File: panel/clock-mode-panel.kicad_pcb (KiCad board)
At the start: 2 copper layers, 40.3 x 128.5 mm, 0 parts

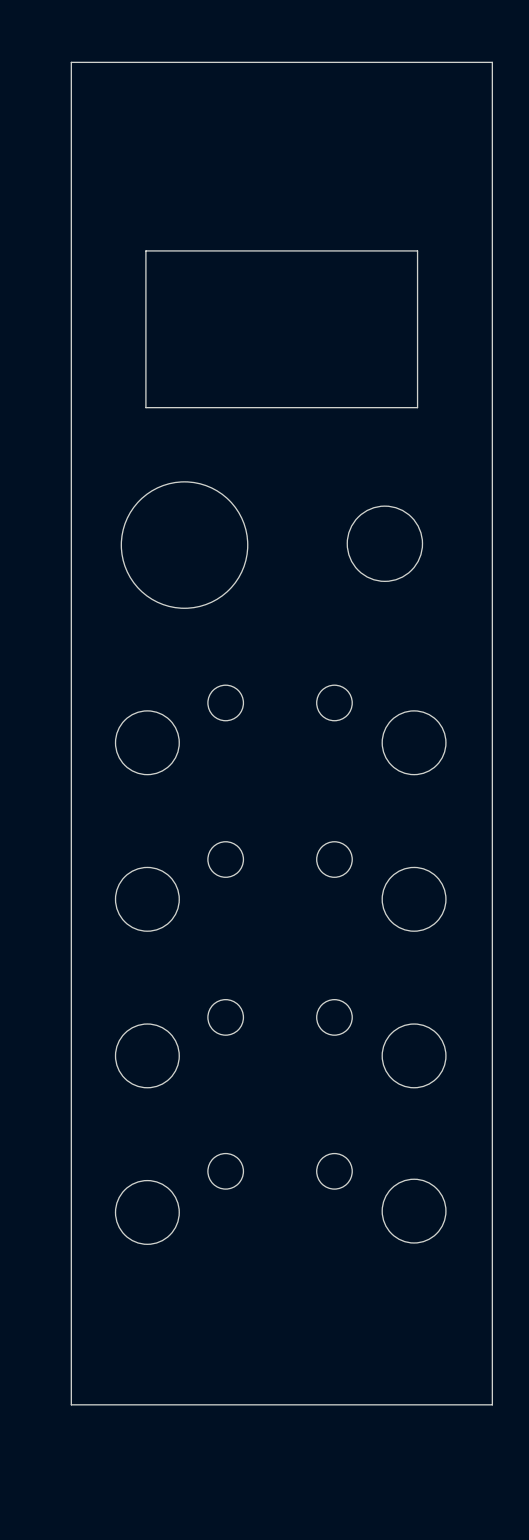
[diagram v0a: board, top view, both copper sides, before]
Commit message: feat: add artwork to panel
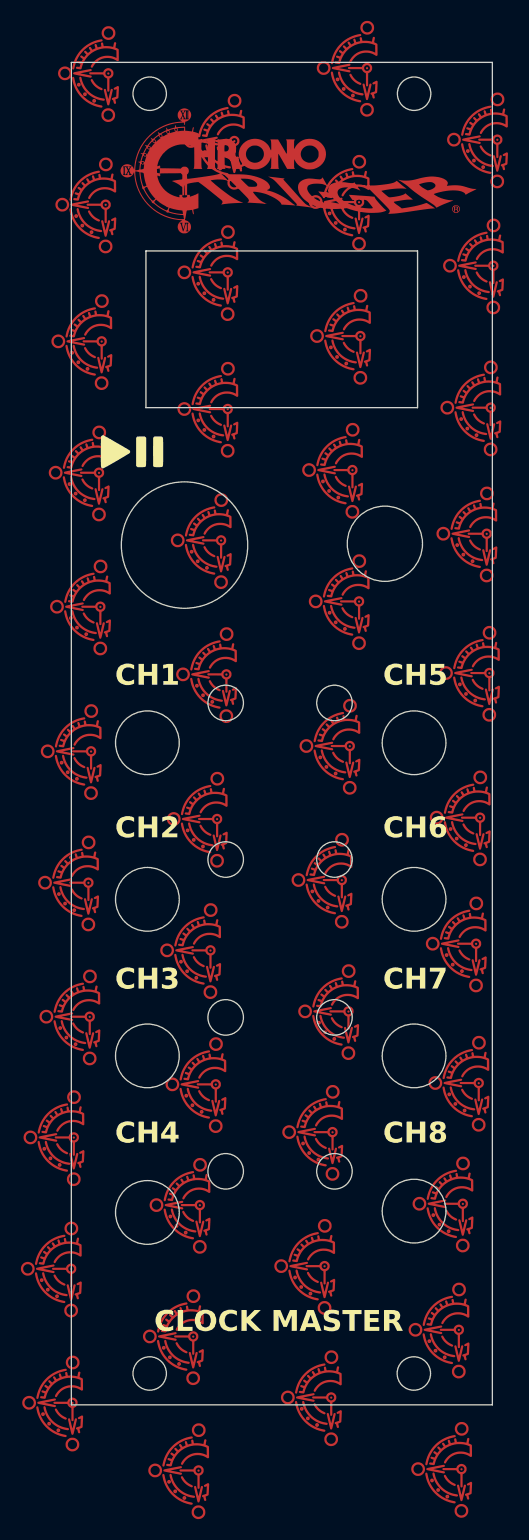
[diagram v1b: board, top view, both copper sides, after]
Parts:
- added G***: LOGO, LOGO, F.Cu at (42.4, 172.3)
- added G***: LOGO, LOGO, F.Cu at (30.2, 153.0)
- added G***: LOGO, LOGO, F.Cu at (70.2, 96.0)
- added G***: LOGO, LOGO, F.Cu at (57.8, 89.2)
- added G***: LOGO, LOGO, F.Cu at (71.0, 45.0)
- added G*** (x2): LOGO, LOGO, F.Cu at (52.8, 47.9)
- added G***: LOGO, LOGO, F.Cu at (37.2, 74.9)
- added G***: LOGO, LOGO, F.Cu at (56.9, 103.0)
- added G***: LOGO, LOGO, F.Cu at (56.1, 115.8)
- added G***: LOGO, LOGO, F.Cu at (33.0, 89.7)
- added G***: LOGO, LOGO, F.Cu at (57.1, 76.6)
- added G***: LOGO, LOGO, F.Cu at (55.2, 140.0)
- added G***: LOGO, LOGO, F.Cu at (44.6, 83.3)
- added G***: LOGO, LOGO, F.Cu at (57.9, 63.8)
- added G***: LOGO, LOGO, F.Cu at (30.5, 140.5)
- added G***: LOGO, LOGO, F.Cu at (67.7, 146.8)
- added G***: LOGO, LOGO, F.Cu at (32.1, 103.5)
- added G***: LOGO, LOGO, F.Cu at (45.1, 96.1)
- added G***: LOGO, LOGO, F.Cu at (30.3, 165.9)
- added G***: LOGO, LOGO, F.Cu at (67.6, 172.2)
- added G***: LOGO, LOGO, F.Cu at (45.8, 45.1)
- added G***: LOGO, LOGO, F.Cu at (33.1, 64.3)
- added G***: LOGO, LOGO, F.Cu at (58.5, 38.1)
- added G***: LOGO, LOGO, F.Cu at (70.0, 82.7)
- added G***: LOGO, LOGO, F.Cu at (54.5, 152.8)
- added G***: LOGO, LOGO, F.Cu at (31.9, 116.1)
- added G***: LOGO, LOGO, F.Cu at (45.2, 70.7)
- added G***: LOGO, LOGO, F.Cu at (69.3, 109.9)
- added G***: LOGO, LOGO, F.Cu at (33.5, 51.2)
- added G***: LOGO, LOGO, F.Cu at (69.0, 121.9)
- added G***: LOGO, LOGO, F.Cu at (43.5, 122.6)
- added G***: LOGO, LOGO, F.Cu at (57.8, 50.9)
- added G***: LOGO, LOGO, F.Cu at (70.6, 57.0)
- added G***: LOGO, LOGO, F.Cu at (32.0, 128.9)
- added G***: LOGO, LOGO, F.Cu at (45.2, 57.7)
- added G***: LOGO, LOGO, F.Cu at (70.4, 70.6)
- added G***: LOGO, LOGO, F.Cu at (69.2, 135.3)
- added G***: LOGO, LOGO, F.Cu at (67.3, 158.9)
- added G***: LOGO, LOGO, F.Cu at (33.8, 38.6)
- added G***: LOGO, LOGO, F.Cu at (44.0, 135.4)
- added G***: LOGO, LOGO, F.Cu at (42.5, 146.9)
- added G***: LOGO, LOGO, F.Cu at (32.9, 76.8)
- added G***: LOGO, LOGO, F.Cu at (44.2, 110.0)
- added G***: LOGO, LOGO, F.Cu at (41.9, 159.5)
- added G***: LOGO, LOGO, F.Cu at (56.7, 128.4)
- added G***: LOGO, LOGO, F.Cu at (55.1, 165.4)
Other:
- outline, holes or cut-outs redrawn
- board text added: "CH1"
- board text added: "CH2"
- board text added: "CH3"
- board text added: "CH4"
- board text added: "CH5"
- board text added: "CH6"
- board text added: "CH7"
- board text added: "CH8"
- board text added: "CLOCK MASTER"
